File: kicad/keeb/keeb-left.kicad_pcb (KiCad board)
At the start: 2 copper layers, 135.4 x 118 mm, 70 parts

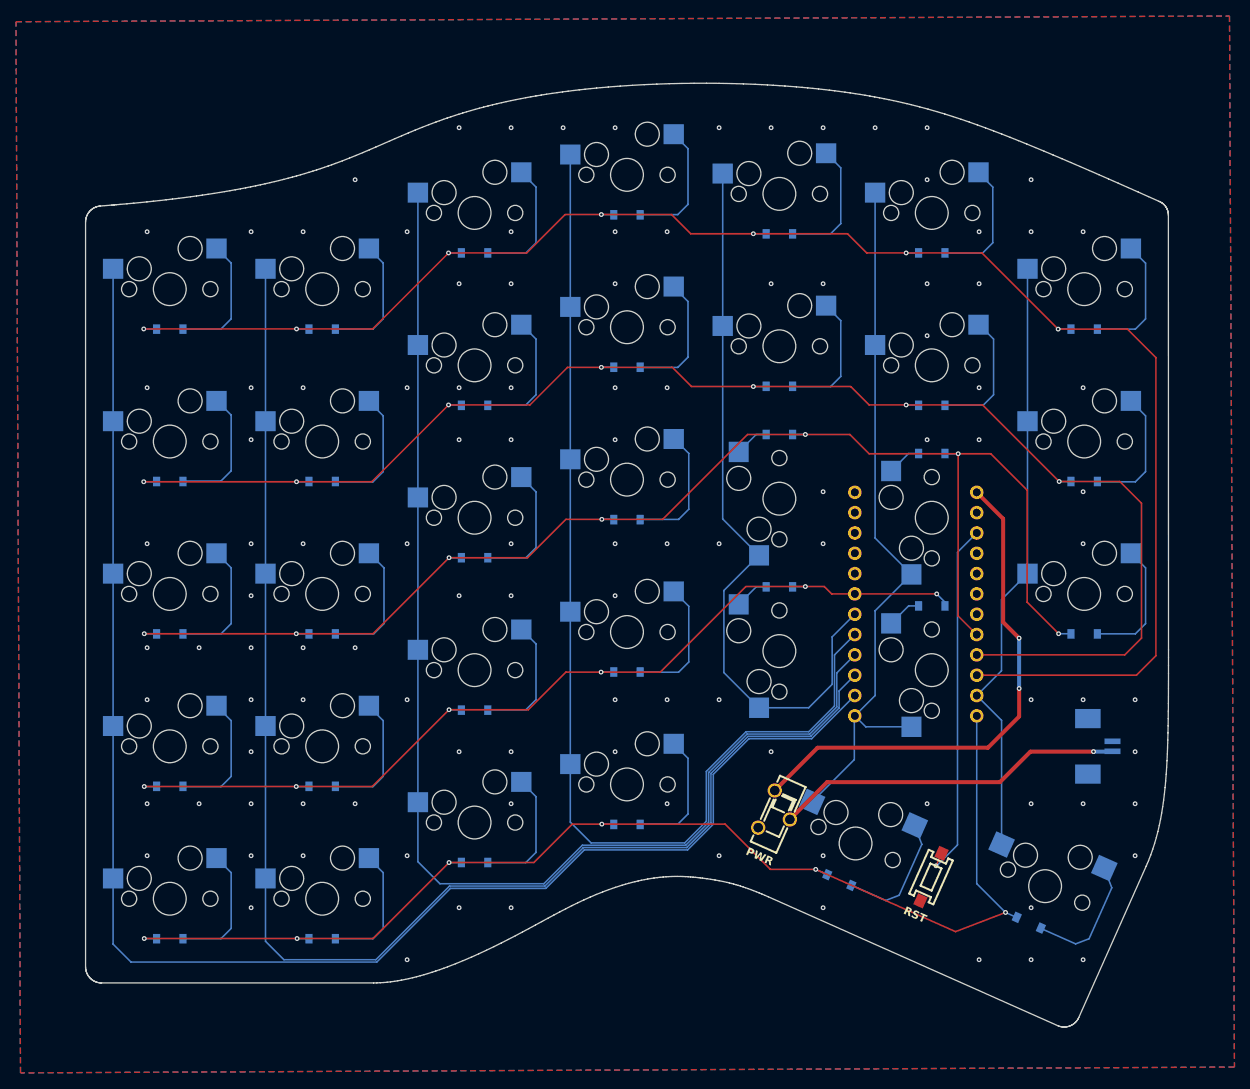
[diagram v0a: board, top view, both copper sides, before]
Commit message: Adding datasheets for switches and connector, updating readme with notes, fixing missing via stitch group on left board
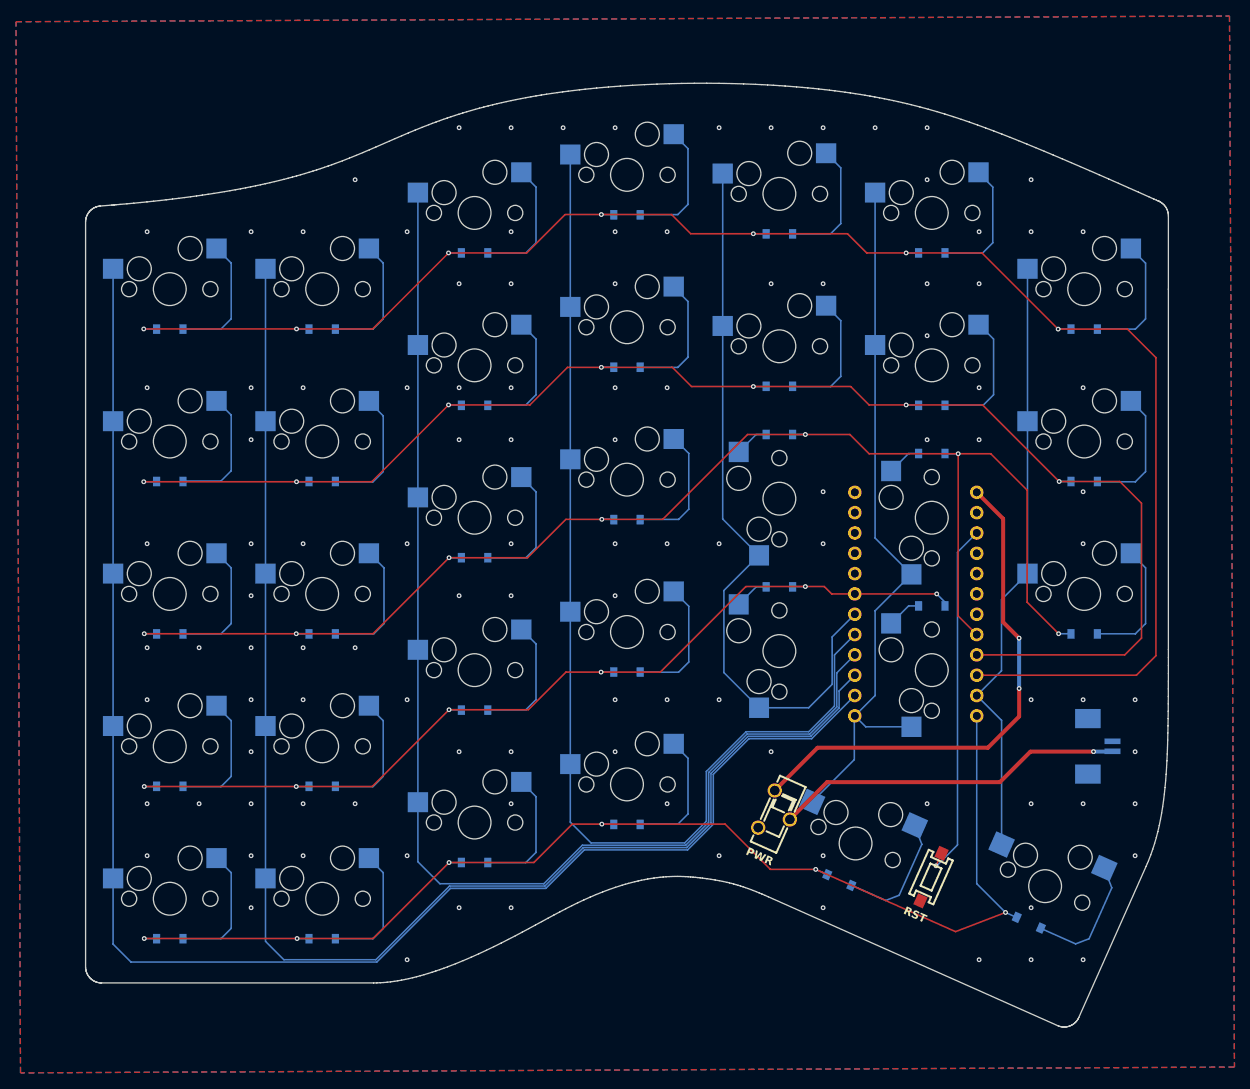
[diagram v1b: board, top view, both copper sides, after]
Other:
- outline, holes or cut-outs redrawn
